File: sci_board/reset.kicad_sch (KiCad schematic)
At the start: 2 parts, among them SW1 EVP-AA602W

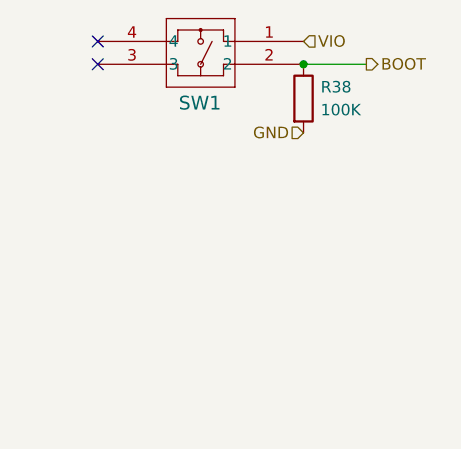
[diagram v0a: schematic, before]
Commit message: add SPI CS and MISO pullups and terminations, remove WD from SCI
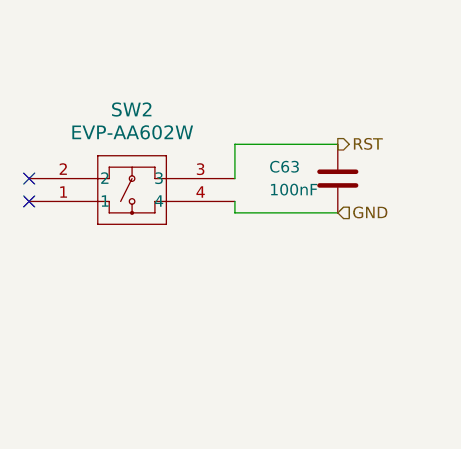
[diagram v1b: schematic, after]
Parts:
- removed R38: 100K, Resistor_SMD:R_0402_1005Metric_Pad0.72x0.64mm_HandSolder, symbol Device:R
- removed SW1: EVP-AA602W, Project:EVP602AA, symbol Project:EVP-AA602W
- added C63: 100nF, Capacitor_SMD:C_0402_1005Metric_Pad0.74x0.62mm_HandSolder, symbol Device:C
- added SW2: EVP-AA602W, Project:EVP602AA, symbol Project:EVP-AA602W
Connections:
- net GND: now also C63.2, SW2.4
- new net RST: C63.1, SW2.3

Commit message: tweaking SCI and AUX for production, using common sheets as much as possible
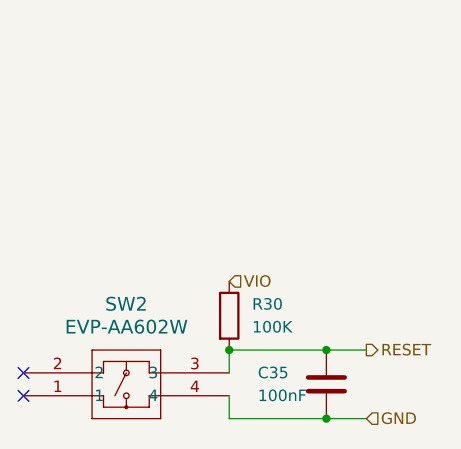
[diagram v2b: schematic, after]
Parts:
- removed C63: 100nF, Capacitor_SMD:C_0402_1005Metric_Pad0.74x0.62mm_HandSolder, symbol Device:C
- added C35: 100nF, Capacitor_SMD:C_0402_1005Metric_Pad0.74x0.62mm_HandSolder, symbol Device:C
- added R30: 100K, Resistor_SMD:R_0402_1005Metric_Pad0.72x0.64mm_HandSolder, symbol Device:R
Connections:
- net GND: now also C35.2
- net RST renamed RESET
- net RESET: now also C35.1, R30.2
- new net VIO: R30.1

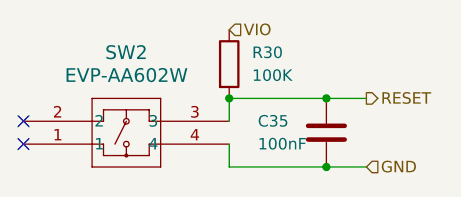
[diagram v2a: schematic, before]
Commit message: clenup BOM for SCI and AUX
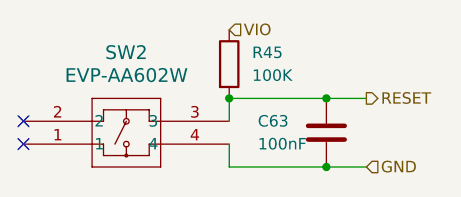
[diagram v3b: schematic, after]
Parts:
- R45: renamed from R30; Manufacturer (none) -> YAGEO; Note (none) -> generic pullup/down; Part Number (none) -> RC0402FR-07100KL; Tolerance (none) -> 1
- renumbered C35 to C63
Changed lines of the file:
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@@
 			)
 		)
-		(property "Description" ""
+		(property "Description" "SWITCH TACTILE SPST-NO 0.02A 15V"
 			(at 132.715 125.095 0)
 			(effects
@@
 			)
 		)
-		(property "MANUFACTURER" ""
-			(at 132.715 125.095 0)
-			(effects
-				(font
-					(size 1.27 1.27)
-				)
-				(hide yes)
-			)
-		)
-		(property "MAXIMUM_PACKAGE_HEIGHT" ""
-			(at 132.715 125.095 0)
-			(effects
-				(font
-					(size 1.27 1.27)
-				)
-				(hide yes)
-			)
-		)
-		(property "Manufactorer" ""
-			(at 132.715 125.095 0)
-			(effects
-				(font
-					(size 1.27 1.27)
-				)
-				(hide yes)
-			)
-		)
-		(property "PARTREV" ""
-			(at 132.715 125.095 0)
-			(effects
-				(font
-					(size 1.27 1.27)
-				)
-				(hide yes)
-			)
-		)
-		(property "STANDARD" ""
-			(at 132.715 125.095 0)
-			(effects
-				(font
-					(size 1.27 1.27)
-				)
-				(hide yes)
-			)
-		)
 		(pin "4"
 		)
@@
 		)
 		(instances
-			(project "sci_board"
-				(path "/85134265-2435-454a-99c4-e49d8e69c5c2/490a0c5b-9225-4953-ad7a-fe6abb29cde0/ff5fe26c-ac2c-4dc8-9dc9-af4e82d95eed"
-					(reference "SW2")
-					(unit 1)
-				)
-			)
 			(project "sci_board"
 				(path "/b4b2c88d-f6cd-4e60-862d-e21f68728580/840799ac-4fe6-4a8e-96a2-299affeec8e4/bc095972-e013-4615-9f72-847fc40745b3"
@@
 		(dnp no)
 		(fields_autoplaced yes)
-		(property "Reference" "R30"
+		(property "Reference" "R45"
 			(at 158.115 114.9349 0)
 			(effects
@@
 			)
 		)
-		(property "Datasheet" "~"
+		(property "Datasheet" "https://www.yageo.com/upload/media/product/products/datasheet/rchip/PYu-RC_Group_51_RoHS_L_12.pdf"
 			(at 155.575 116.205 0)
 			(effects
@@
 			)
 		)
+		(property "Manufacturer" "YAGEO"
+			(at 155.575 116.205 0)
+			(effects
+				(font
+					(size 1.27 1.27)
+				)
+				(hide yes)
+			)
+		)
+		(property "Note" "generic pullup/down"
+			(at 155.575 116.205 0)
+			(effects
+				(font
+					(size 1.27 1.27)
+				)
+				(hide yes)
+			)
+		)
+		(property "Part Number" "RC0402FR-07100KL"
+			(at 155.575 116.205 0)
+			(effects
+				(font
+					(size 1.27 1.27)
+				)
+				(hide yes)
+			)
+		)
+		(property "Tolerance" "1"
+			(at 155.575 116.205 0)
+			(effects
+				(font
+					(size 1.27 1.27)
+				)
+				(hide yes)
+			)
+		)
 		(pin "2"
 		)
@@
 		)
 		(instances
-			(project "sci_board"
-				(path "/85134265-2435-454a-99c4-e49d8e69c5c2/490a0c5b-9225-4953-ad7a-fe6abb29cde0/ff5fe26c-ac2c-4dc8-9dc9-af4e82d95eed"
-					(reference "R30")
-					(unit 1)
-				)
-			)
 			(project "sci_board"
 				(path "/b4b2c88d-f6cd-4e60-862d-e21f68728580/840799ac-4fe6-4a8e-96a2-299affeec8e4/bc095972-e013-4615-9f72-847fc40745b3"
@@
 		(on_board yes)
 		(dnp no)
-		(property "Reference" "C35"
+		(property "Reference" "C63"
 			(at 158.75 122.555 0)
 			(effects
@@
 			)
 		)
-		(property "Description" ""
+		(property "Description" "Unpolarized capacitor"
 			(at 166.37 123.825 0)
 			(effects
@@
 		)
 		(property "Manufacturer" "Murata"
-			(at 166.37 123.825 0)
-			(effects
-				(font
-					(size 1.27 1.27)
-				)
-				(hide yes)
-			)
-		)
-		(property "MANUFACTURER" ""
-			(at 166.37 123.825 0)
-			(effects
-				(font
-					(size 1.27 1.27)
-				)
-				(hide yes)
-			)
-		)
-		(property "MAXIMUM_PACKAGE_HEIGHT" ""
-			(at 166.37 123.825 0)
-			(effects
-				(font
-					(size 1.27 1.27)
-				)
-				(hide yes)
-			)
-		)
-		(property "Manufactorer" ""
-			(at 166.37 123.825 0)
-			(effects
-				(font
-					(size 1.27 1.27)
-				)
-				(hide yes)
-			)
-		)
-		(property "PARTREV" ""
-			(at 166.37 123.825 0)
-			(effects
-				(font
-					(size 1.27 1.27)
-				)
-				(hide yes)
-			)
-		)
-		(property "STANDARD" ""
 			(at 166.37 123.825 0)
 			(effects
@@
 		(instances
 			(project "sci_board"
-				(path "/85134265-2435-454a-99c4-e49d8e69c5c2/490a0c5b-9225-4953-ad7a-fe6abb29cde0/ff5fe26c-ac2c-4dc8-9dc9-af4e82d95eed"
-					(reference "C35")
-					(unit 1)
-				)
-			)
-			(project "sci_board"
 				(path "/b4b2c88d-f6cd-4e60-862d-e21f68728580/840799ac-4fe6-4a8e-96a2-299affeec8e4/bc095972-e013-4615-9f72-847fc40745b3"

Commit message: cleaning up bom: remove main camera port since it has not pullups and capacitors, correcting some errors in camera switch
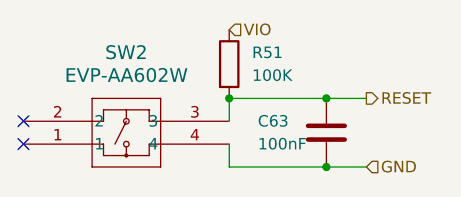
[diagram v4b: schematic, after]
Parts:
- renumbered R45 to R51
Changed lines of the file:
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@@
 		(dnp no)
 		(fields_autoplaced yes)
-		(property "Reference" "R45"
+		(property "Reference" "R51"
 			(at 158.115 114.9349 0)
 			(effects
@@
 			(project "sci_board"
 				(path "/b4b2c88d-f6cd-4e60-862d-e21f68728580/840799ac-4fe6-4a8e-96a2-299affeec8e4/bc095972-e013-4615-9f72-847fc40745b3"
-					(reference "R45")
+					(reference "R51")
 					(unit 1)
 				)

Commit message: QC, add second 3V regulator to AUX, INT pullups on AUX SCI AVI
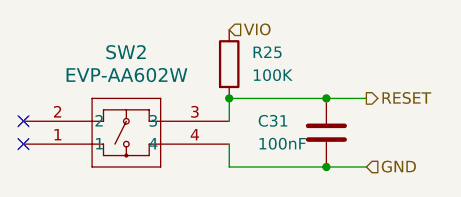
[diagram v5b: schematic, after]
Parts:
- SW2: footprint Project:EVP602AA -> Common:EVP602AA
- renumbered C63 to C31, R51 to R25
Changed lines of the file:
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@@
 			)
 		)
-		(property "Footprint" "Project:EVP602AA"
+		(property "Footprint" "Common:EVP602AA"
 			(at 132.715 125.095 0)
 			(effects
@@
 		)
 		(instances
+			(project "aux_board"
+				(path "/85134265-2435-454a-99c4-e49d8e69c5c2/490a0c5b-9225-4953-ad7a-fe6abb29cde0/ff5fe26c-ac2c-4dc8-9dc9-af4e82d95eed"
+					(reference "SW2")
+					(unit 1)
+				)
+			)
 			(project "sci_board"
 				(path "/b4b2c88d-f6cd-4e60-862d-e21f68728580/840799ac-4fe6-4a8e-96a2-299affeec8e4/bc095972-e013-4615-9f72-847fc40745b3"
@@
 		(dnp no)
 		(fields_autoplaced yes)
-		(property "Reference" "R51"
+		(property "Reference" "R25"
 			(at 158.115 114.9349 0)
 			(effects
@@
 		)
 		(instances
+			(project "aux_board"
+				(path "/85134265-2435-454a-99c4-e49d8e69c5c2/490a0c5b-9225-4953-ad7a-fe6abb29cde0/ff5fe26c-ac2c-4dc8-9dc9-af4e82d95eed"
+					(reference "R25")
+					(unit 1)
+				)
+			)
 			(project "sci_board"
 				(path "/b4b2c88d-f6cd-4e60-862d-e21f68728580/840799ac-4fe6-4a8e-96a2-299affeec8e4/bc095972-e013-4615-9f72-847fc40745b3"
@@
 		(on_board yes)
 		(dnp no)
-		(property "Reference" "C63"
+		(property "Reference" "C31"
 			(at 158.75 122.555 0)
 			(effects
@@
 		)
 		(instances
+			(project "aux_board"
+				(path "/85134265-2435-454a-99c4-e49d8e69c5c2/490a0c5b-9225-4953-ad7a-fe6abb29cde0/ff5fe26c-ac2c-4dc8-9dc9-af4e82d95eed"
+					(reference "C31")
+					(unit 1)
+				)
+			)
 			(project "sci_board"
 				(path "/b4b2c88d-f6cd-4e60-862d-e21f68728580/840799ac-4fe6-4a8e-96a2-299affeec8e4/bc095972-e013-4615-9f72-847fc40745b3"

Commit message: propate the changes to RF
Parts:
- SW2: symbol Project:EVP-AA602W -> Common:EVP-AA602W
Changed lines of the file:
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@@
 	)
 	(symbol
-		(lib_name "EVP-AA602W_1")
-		(lib_id "Project:EVP-AA602W")
+		(lib_id "Common:EVP-AA602W")
 		(at 132.715 125.095 0)
 		(mirror x)
@@
 		(fields_autoplaced yes)
 		(property "Reference" "SW2"
-			(at 144.145 114.935 0)
+			(at 144.145 115.57 0)
 			(effects
 				(font
@@
 		)
 		(property "Value" "EVP-AA602W"
-			(at 144.145 117.475 0)
+			(at 144.145 118.11 0)
 			(effects
 				(font
@@
 			(project "aux_board"
 				(path "/85134265-2435-454a-99c4-e49d8e69c5c2/490a0c5b-9225-4953-ad7a-fe6abb29cde0/ff5fe26c-ac2c-4dc8-9dc9-af4e82d95eed"
+					(reference "SW2")
+					(unit 1)
+				)
+			)
+			(project "aux_board"
+				(path "/a863a5ec-a5d4-4f54-be53-e8c01d5e3ac4/53f12969-e593-459a-9671-cc23a5a9aea0/f4ff56ce-2fa2-4b99-a709-c113709260c1/4970b3a5-e48c-4e2f-a825-cd6a14be31b4"
 					(reference "SW2")
 					(unit 1)
@@
 				)
 			)
+			(project "aux_board"
+				(path "/a863a5ec-a5d4-4f54-be53-e8c01d5e3ac4/53f12969-e593-459a-9671-cc23a5a9aea0/f4ff56ce-2fa2-4b99-a709-c113709260c1/4970b3a5-e48c-4e2f-a825-cd6a14be31b4"
+					(reference "R36")
+					(unit 1)
+				)
+			)
 			(project "sci_board"
 				(path "/b4b2c88d-f6cd-4e60-862d-e21f68728580/840799ac-4fe6-4a8e-96a2-299affeec8e4/bc095972-e013-4615-9f72-847fc40745b3"
@@
 					(unit 1)
 				)
+			)
+			(project "aux_board"
+				(path "/a863a5ec-a5d4-4f54-be53-e8c01d5e3ac4/53f12969-e593-459a-9671-cc23a5a9aea0/f4ff56ce-2fa2-4b99-a709-c113709260c1/4970b3a5-e48c-4e2f-a825-cd6a14be31b4"
+					(reference "C59")
+					(unit 1)
+				)

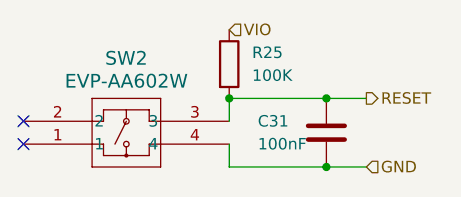
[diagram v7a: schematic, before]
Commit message: local switches and monitors for SCI and RF
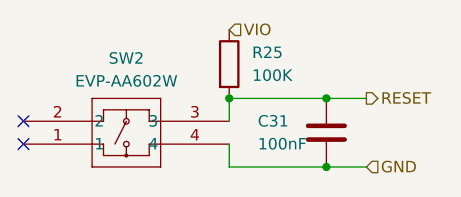
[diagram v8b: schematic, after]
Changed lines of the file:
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@@
 			(effects
 				(font
-					(size 1.524 1.524)
+					(size 1.27 1.27)
 				)
 			)
@@
 			(effects
 				(font
-					(size 1.524 1.524)
+					(size 1.27 1.27)
 				)
 			)
@@
 			(project "aux_board"
 				(path "/85134265-2435-454a-99c4-e49d8e69c5c2/490a0c5b-9225-4953-ad7a-fe6abb29cde0/ff5fe26c-ac2c-4dc8-9dc9-af4e82d95eed"
+					(reference "SW2")
+					(unit 1)
+				)
+			)
+			(project "openlst-hw"
+				(path "/a863a5ec-a5d4-4f54-be53-e8c01d5e3ac4/53f12969-e593-459a-9671-cc23a5a9aea0/f4ff56ce-2fa2-4b99-a709-c113709260c1/4970b3a5-e48c-4e2f-a825-cd6a14be31b4"
 					(reference "SW2")
 					(unit 1)
@@
 				)
 			)
+			(project "openlst-hw"
+				(path "/a863a5ec-a5d4-4f54-be53-e8c01d5e3ac4/53f12969-e593-459a-9671-cc23a5a9aea0/f4ff56ce-2fa2-4b99-a709-c113709260c1/4970b3a5-e48c-4e2f-a825-cd6a14be31b4"
+					(reference "R50")
+					(unit 1)
+				)
+			)
 			(project "sci_board"
 				(path "/b4b2c88d-f6cd-4e60-862d-e21f68728580/840799ac-4fe6-4a8e-96a2-299affeec8e4/bc095972-e013-4615-9f72-847fc40745b3"
-					(reference "R51")
+					(reference "R58")
 					(unit 1)
 				)
@@
 				)
 			)
+			(project "openlst-hw"
+				(path "/a863a5ec-a5d4-4f54-be53-e8c01d5e3ac4/53f12969-e593-459a-9671-cc23a5a9aea0/f4ff56ce-2fa2-4b99-a709-c113709260c1/4970b3a5-e48c-4e2f-a825-cd6a14be31b4"
+					(reference "C69")
+					(unit 1)
+				)
+			)
 			(project "sci_board"
 				(path "/b4b2c88d-f6cd-4e60-862d-e21f68728580/840799ac-4fe6-4a8e-96a2-299affeec8e4/bc095972-e013-4615-9f72-847fc40745b3"
-					(reference "C63")
-					(unit 1)
-				)
+					(reference "C69")
+					(unit 1)
+				)
